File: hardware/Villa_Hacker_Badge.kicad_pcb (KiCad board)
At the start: 2 copper layers, 45.1 x 50 mm, 24 parts, among them J1 Conn_02x03_Odd_Even, SW1 SW_RST, SW2 On, U1 PY32F002AA15M6TU

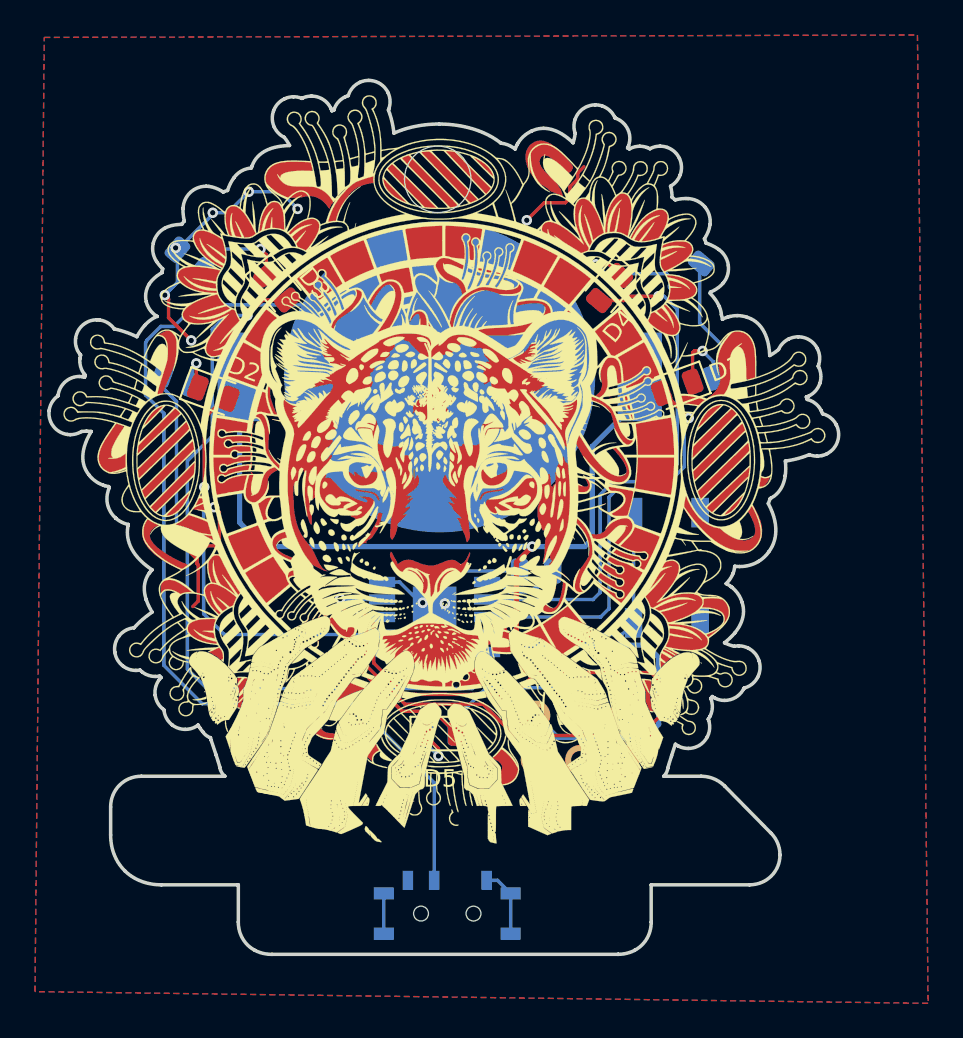
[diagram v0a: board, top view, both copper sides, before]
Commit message: fix(Hw):Move_Switch
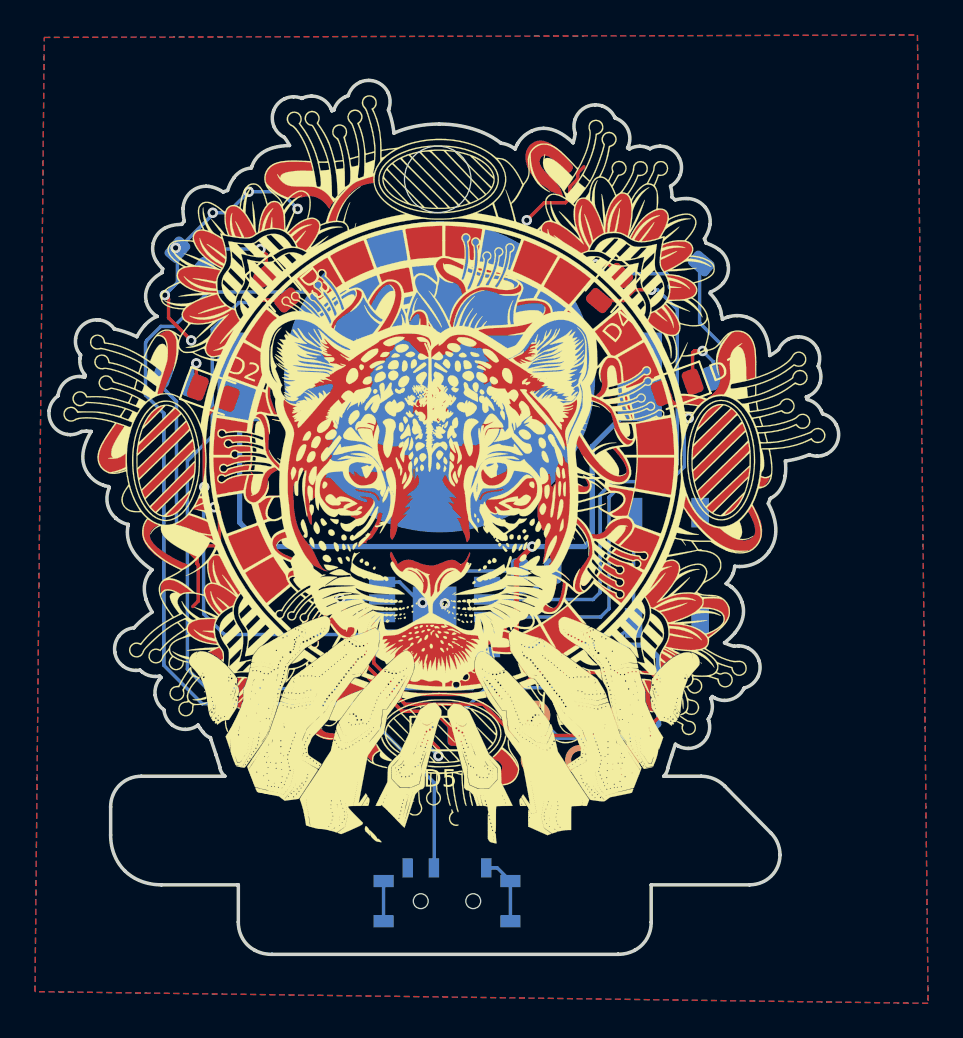
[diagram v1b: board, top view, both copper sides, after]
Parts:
- moved SW2 0.71 mm to (79.4, 80.0)
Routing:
- net GND: track 75.2 -> 77.0 mm
